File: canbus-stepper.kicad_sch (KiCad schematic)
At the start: 56 parts, among them J1 TYPE-C USB SOCKET, J2 Motor Output, J3 CAN Daisy-Chain 1, J4 CAN Daisy-Chain 2, J5 Qwiic I2C, J6 AUX Port, J7 SFV30R-2STBE1HLF (30-Pin OLED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, J8 24V Power Input Terminal, J9 24V Power Output Terminal, SW1 SW_Push, SW2 SW_Push, SW3 SW_Push, SW4 SW_Push, U1 ESP32-S3-WROOM-1, U2 TMC2209, U3 MT6701, U4 SN65HVD230, U5 MP2315, U6 ME6211C33

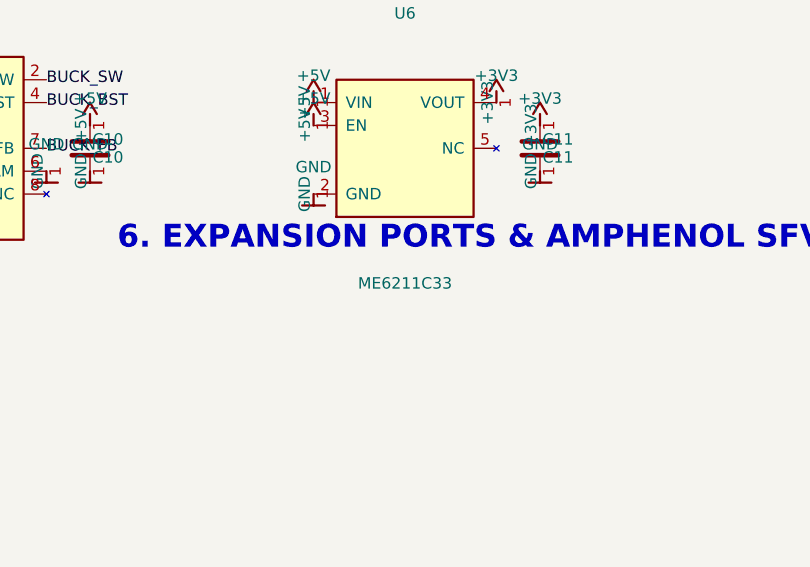
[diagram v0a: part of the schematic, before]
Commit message: Updated SW1-SW4, U6, J2 footprints & values in both schematic and PCB files
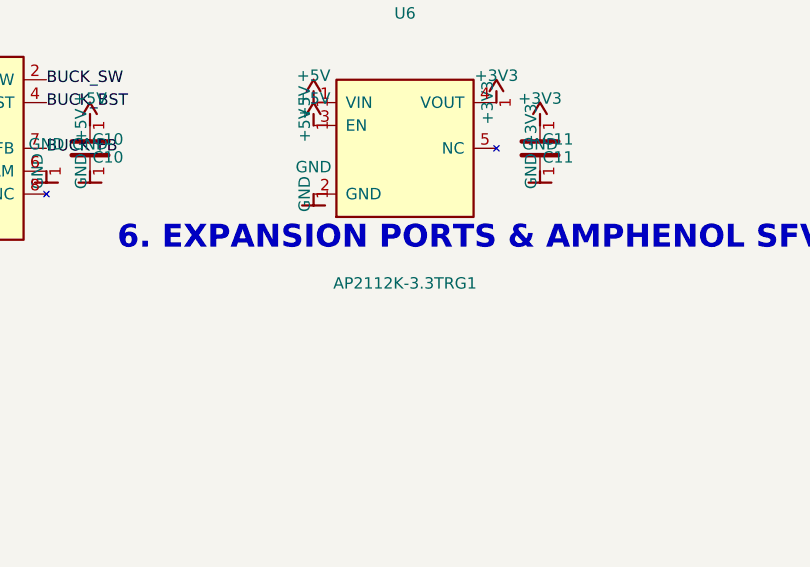
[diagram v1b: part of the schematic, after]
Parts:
- SW1, SW2: footprint Button_Switch_SMD:SW_Push_1P1T_NO_E-Switch_TL3301NxxxxxG -> CANBUS-Stepper:SW_TL3365AF180QG
- SW3, SW4: footprint Button_Switch_SMD:SW_Push_1P1T_NO_E-Switch_TL3301NxxxxxG -> CANBUS-Stepper:SW_TS31-46-35-BK-B-160-RA-SMT-TR
- U6: value ME6211C33 -> AP2112K-3.3TRG1
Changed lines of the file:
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@@
 			)
 		)
-		(property "Value" "ME6211C33"
+		(property "Value" "AP2112K-3.3TRG1"
 			(at 254.79 268.19 0)
 			(show_name no)
@@
 			)
 		)
-		(property "Footprint" "Button_Switch_SMD:SW_Push_1P1T_NO_E-Switch_TL3301NxxxxxG"
+		(property "Footprint" "CANBUS-Stepper:SW_TS31-46-35-BK-B-160-RA-SMT-TR"
 			(at 179.79 113.19 0)
 			(hide yes)
@@
 			)
 		)
-		(property "Footprint" "Button_Switch_SMD:SW_Push_1P1T_NO_E-Switch_TL3301NxxxxxG"
+		(property "Footprint" "CANBUS-Stepper:SW_TS31-46-35-BK-B-160-RA-SMT-TR"
 			(at 179.79 103.19 0)
 			(hide yes)
@@
 			)
 		)
-		(property "Footprint" "Button_Switch_SMD:SW_Push_1P1T_NO_E-Switch_TL3301NxxxxxG"
+		(property "Footprint" "CANBUS-Stepper:SW_TL3365AF180QG"
 			(at 264.79 170.69 0)
 			(hide yes)
@@
 			)
 		)
-		(property "Footprint" "Button_Switch_SMD:SW_Push_1P1T_NO_E-Switch_TL3301NxxxxxG"
+		(property "Footprint" "CANBUS-Stepper:SW_TL3365AF180QG"
 			(at 264.79 168.19 0)
 			(hide yes)

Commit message: feat: complete hardware schematic fixes, 0603 footprint optimizations, AS5600 encoder, TCAN1051V transceiver, and IPC-2221 design rules
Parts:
- C1, C11, C12, C13, C14, C15, C2, C3, C4, C5, C6, C7, C8: footprint Capacitor_SMD:C_0805_2012Metric -> Capacitor_SMD:C_0603_1608Metric
- C9: footprint Capacitor_SMD:C_0805_2012Metric -> Capacitor_SMD:C_1206_3216Metric
- R1, R10, R11, R12, R13, R14, R15, R16, R17, R2, R3, R6, R7, R8, R9: footprint Resistor_SMD:R_0805_2012Metric -> Resistor_SMD:R_0603_1608Metric
- R4, R5: footprint Resistor_SMD:R_0805_2012Metric -> Resistor_SMD:R_1206_3216Metric
- U3: value MT6701 -> AS5600-ASOT
- U4: value SN65HVD230 -> TCAN1051VDRBTQ1; footprint Package_SO:SOIC-8_3.9x4.9mm_P1.27mm -> CANBUS-Stepper:TCAN1051VDRBTQ1
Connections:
- net EN: now also SW1.1; no longer SW3.1
- net IO0: now also SW2.1; no longer SW4.1
- net SW1: now also SW3.1; no longer SW1.1
- net SW2: now also SW4.1; no longer SW2.1
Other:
- moved on the sheet: U1

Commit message: feat: update schematic and pcb layout design files
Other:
- moved on the sheet: C1, C10, C11, C12, C13, C14, C15, C2, C3, C4, C5, C6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

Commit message: feat: set exact datasheet values for all passive resistors (R1-R17) and capacitors (C1-C15)
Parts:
- C1: value C1 -> 1uF
- C10: value C10 -> 22uF
- C11: value C11 -> 1uF
- C12: value C12 -> 1uF
- C13: value C13 -> 1uF
- C14: value C14 -> 4.7uF
- C15: value C15 -> 4.7uF
- C2: value C2 -> 100nF
- C3: value C3 -> 100nF 50V
- C4: value C4 -> 100nF 50V
- C5: value C5 -> 22nF 50V
- C6: value C6 -> 100nF
- C7: value C7 -> 100nF
- C8: value C8 -> 100nF
- C9: value C9 -> 10uF 50V
- R1: value R1 -> 10k
- R10: value R10 -> 100k
- R11: value R11 -> 10k
- R12: value R12 -> 10k
- R13: value R13 -> 1k
- R14: value R14 -> 1k
- R15: value R15 -> 5.1k
- R16: value R16 -> 5.1k
- R17: value R17 -> 390k
- R2: value R2 -> 10k
- R3: value R3 -> 10k
- R4: value R4 -> 0.11R
- R5: value R5 -> 0.11R
- R6: value R6 -> 1k
- R7: value R7 -> 4.7k
- R8: value R8 -> 4.7k
- R9: value R9 -> 120R
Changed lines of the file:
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@@
 			)
 		)
-		(property "Value" "R17"
+		(property "Value" "390k"
 			(at 487.93 253.25 0)
 			(show_name no)
@@
 			)
 		)
-		(property "Value" "R9"
+		(property "Value" "120R"
 			(at 337.91 195.15 0)
 			(show_name no)
@@
 			)
 		)
-		(property "Value" "R10"
+		(property "Value" "100k"
 			(at 82.89 112.44 0)
 			(show_name no)
@@
 			)
 		)
-		(property "Value" "C13"
+		(property "Value" "1uF"
 			(at 497.93 233.25 0)
 			(show_name no)
@@
 			)
 		)
-		(property "Value" "C4"
+		(property "Value" "100nF 50V"
 			(at 282.59 61.96 0)
 			(show_name no)
@@
 			)
 		)
-		(property "Value" "R11"
+		(property "Value" "10k"
 			(at 69.31 110.22 0)
 			(show_name no)
@@
 			)
 		)
-		(property "Value" "R1"
+		(property "Value" "10k"
 			(at 102.89 72.44 0)
 			(show_name no)
@@
 			)
 		)
-		(property "Value" "C2"
+		(property "Value" "100nF"
 			(at 117.57 92.44 0)
 			(show_name no)
@@
 			)
 		)
-		(property "Value" "C7"
+		(property "Value" "100nF"
 			(at 469.36 74.66 0)
 			(show_name no)
@@
 			)
 		)
-		(property "Value" "R2"
+		(property "Value" "10k"
 			(at 102.89 82.44 0)
 			(show_name no)
@@
 			)
 		)
-		(property "Value" "R16"
+		(property "Value" "5.1k"
 			(at 57.88 82.28 0)
 			(show_name no)
@@
 			)
 		)
-		(property "Value" "C6"
+		(property "Value" "100nF"
 			(at 287.59 61.96 0)
 			(show_name no)
@@
 			)
 		)
-		(property "Value" "R14"
+		(property "Value" "1k"
 			(at 211.55 108.95 0)
 			(show_name no)
@@
 			)
 		)
-		(property "Value" "R13"
+		(property "Value" "1k"
 			(at 202.66 108.95 0)
 			(show_name no)
@@
 			)
 		)
-		(property "Value" "C11"
+		(property "Value" "1uF"
 			(at 236.71 200.39 0)
 			(show_name no)
@@
 			)
 		)
-		(property "Value" "C1"
+		(property "Value" "1uF"
 			(at 117.57 70.85 0)
 			(show_name no)
@@
 			)
 		)
-		(property "Value" "C14"
+		(property "Value" "4.7uF"
 			(at 502.93 253.25 0)
 			(show_name no)
@@
 			)
 		)
-		(property "Value" "C15"
+		(property "Value" "4.7uF"
 			(at 507.93 253.25 0)
 			(show_name no)
@@
 			)
 		)
-		(property "Value" "C5"
+		(property "Value" "22nF 50V"
 			(at 356.33 67.04 0)
 			(show_name no)
@@
 			)
 		)
-		(property "Value" "R7"
+		(property "Value" "4.7k"
 			(at 518.89 74.66 0)
 			(show_name no)
@@
 			)
 		)
-		(property "Value" "R5"
+		(property "Value" "0.11R"
 			(at 370.3 96.25 0)
 			(show_name no)
@@
 			)
 		)
-		(property "Value" "C10"
+		(property "Value" "22uF"
 			(at 180.83 202.93 0)
 			(show_name no)
@@
 			)
 		)
-		(property "Value" "C8"
+		(property "Value" "100nF"
 			(at 297.91 185.15 0)
 			(show_name no)
@@
 			)
 		)
-		(property "Value" "R8"
+		(property "Value" "4.7k"
 			(at 523.89 74.66 0)
 			(show_name no)
@@
 			)
 		)
-		(property "Value" "R12"
+		(property "Value" "10k"
 			(at 102.89 112.44 0)
 			(show_name no)
@@
 			)
 		)
-		(property "Value" "R15"
+		(property "Value" "5.1k"
 			(at 46.45 82.28 0)
 			(show_name no)
@@
 			)
 		)
-		(property "Value" "R4"
+		(property "Value" "0.11R"
 			(at 358.87 96.25 0)
 			(show_name no)
@@
 			)
 		)
-		(property "Value" "C3"
+		(property "Value" "100nF 50V"
 			(at 277.59 61.96 0)
 			(show_name no)
@@
 			)
 		)
-		(property "Value" "R3"
+		(property "Value" "10k"
 			(at 102.89 92.44 0)
 			(show_name no)
@@
 			)
 		)
-		(property "Value" "R6"
+		(property "Value" "1k"
 			(at 281.4 81.01 0)
 			(show_name no)
@@
 			)
 		)
-		(property "Value" "C9"
+		(property "Value" "10uF 50V"
 			(at 155.83 202.93 0)
 			(show_name no)
@@
 			)
 		)
-		(property "Value" "C12"
+		(property "Value" "1uF"
 			(at 492.93 233.25 0)
 			(show_name no)

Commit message: feat: add 24V PPTC fuse, P-FET reverse polarity protection, USB PPTC fuse, CAN TVS, and USB ESD arrays
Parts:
- added D4: PESD1CAN, Package_TO_SOT_SMD:SOT-23, symbol Power_Protection:PESD1CAN
- added D5: BZX84C12V, Diode_SMD:D_SOT-23_ANK, symbol Device:D_Zener
- added F1: 3.5A 30V PPTC, Fuse:Fuse_1812_4532Metric, symbol Device:Polyfuse
- added F2: 500mA 16V PPTC, Fuse:Fuse_0805_2012Metric, symbol Device:Polyfuse
- added Q1: AO4407A, Package_SO:SOIC-8_3.9x4.9mm_P1.27mm, symbol Device:Q_PMOS_GDS
- added R18: 10k, Resistor_SMD:R_0603_1608Metric, symbol Device:R
- added U7: USBLC6-2SC6, Package_TO_SOT_SMD:SOT-23-6, symbol Power_Protection:USBLC6-2SC6
